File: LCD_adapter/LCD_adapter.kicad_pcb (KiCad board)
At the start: 2 copper layers, 24.8 x 52.1 mm, 3 parts, among them U1 RC1602A

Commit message: version 1 complete
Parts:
- added J1: Conn_01x15_Male, Connector_PinHeader_2.54mm:PinHeader_1x15_P2.54mm_Vertical, F.Cu at (153.7, 64.8)
- added J2: Conn_01x15_Male, Connector_PinHeader_2.54mm:PinHeader_1x15_P2.54mm_Vertical, F.Cu at (163.8, 64.8)
- added REF**: MountingHole_3mm, MountingHole:MountingHole_3mm, F.Cu at (172.0, 61.9)
- added REF**: MountingHole_3mm, MountingHole:MountingHole_3mm, F.Cu at (172.0, 113.7)
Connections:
- A1 pad 1: Net-(A1-Pad1) -> /D1
- A1 pad 10: Net-(A1-Pad10) -> /D7
- A1 pad 11: Net-(A1-Pad11) -> /D8
- A1 pad 12: Net-(A1-Pad12) -> /D9
- A1 pad 13: Net-(A1-Pad13) -> /D10
- A1 pad 16: Net-(A1-Pad16) -> /D13
- A1 pad 17: Net-(A1-Pad17) -> /3V3
- A1 pad 18: Net-(A1-Pad18) -> /AREF
- A1 pad 19: Net-(A1-Pad19) -> /A0
- A1 pad 2: Net-(A1-Pad2) -> /D0
- A1 pad 20: Net-(A1-Pad20) -> /A1
- A1 pad 21: Net-(A1-Pad21) -> /A2
- A1 pad 22: Net-(A1-Pad22) -> /A3
- A1 pad 23: Net-(A1-Pad23) -> /A4
- A1 pad 24: Net-(A1-Pad24) -> /A5
- A1 pad 25: Net-(A1-Pad25) -> /A6
- A1 pad 26: Net-(A1-Pad26) -> /A7
- A1 pad 28: Net-(A1-Pad28) -> /nRST
- A1 pad 3: Net-(A1-Pad3) -> /nRST
- A1 pad 30: Net-(A1-Pad30) -> /Vin
- A1 pad 9: Net-(A1-Pad9) -> /D6
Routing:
- net /nRST: track 0.00 -> 5.08 mm
- net VDD: track 68.1 -> 70.7 mm
- net /D3: track 15.0 -> 17.6 mm
- net /D2: track 15.0 -> 17.6 mm
- net /D12: track 15.0 -> 17.6 mm
- net /Vin: track 0.00 -> 2.54 mm
- net /D9: track 0.00 -> 2.54 mm
- net /D8: track 0.00 -> 2.54 mm, vias 0 -> 1
- net /D7: track 0.00 -> 2.54 mm
- net /D6: track 0.00 -> 2.54 mm
- net /D4: track 15.0 -> 17.6 mm
- net /D13: track 0.00 -> 2.54 mm
- net /D11: track 17.6 -> 20.1 mm
- net /D10: track 0.00 -> 2.54 mm
- net /D1: track 0.00 -> 2.54 mm
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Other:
- board size 24.8 x 52.1 mm -> 26 x 59.1 mm
- board text added: "3V3"
- board text added: "5V"
- board text added: "A0"
- board text added: "A1"
- board text added: "A2"
- board text added: "A3"
- board text added: "A4"
- board text added: "A5"
- board text added: "A6"
- board text added: "A7"
- board text added: "BJI inc. - nano2LCD adapter"
- board text added: "D10"
- board text added: "D11"
- board text added: "D12"
- board text added: "D13"
- board text added: "D2"
- board text added: "D3"
- board text added: "D4"
- board text added: "D5"
- board text added: "D6"
- board text added: "D7"
- board text added: "D8"
- board text added: "D9"
- board text added: "GND"
- board text added: "REF"
- board text added: "RST"
- board text added: "RXD"
- board text added: "TXD"
- board text added: "VIN"

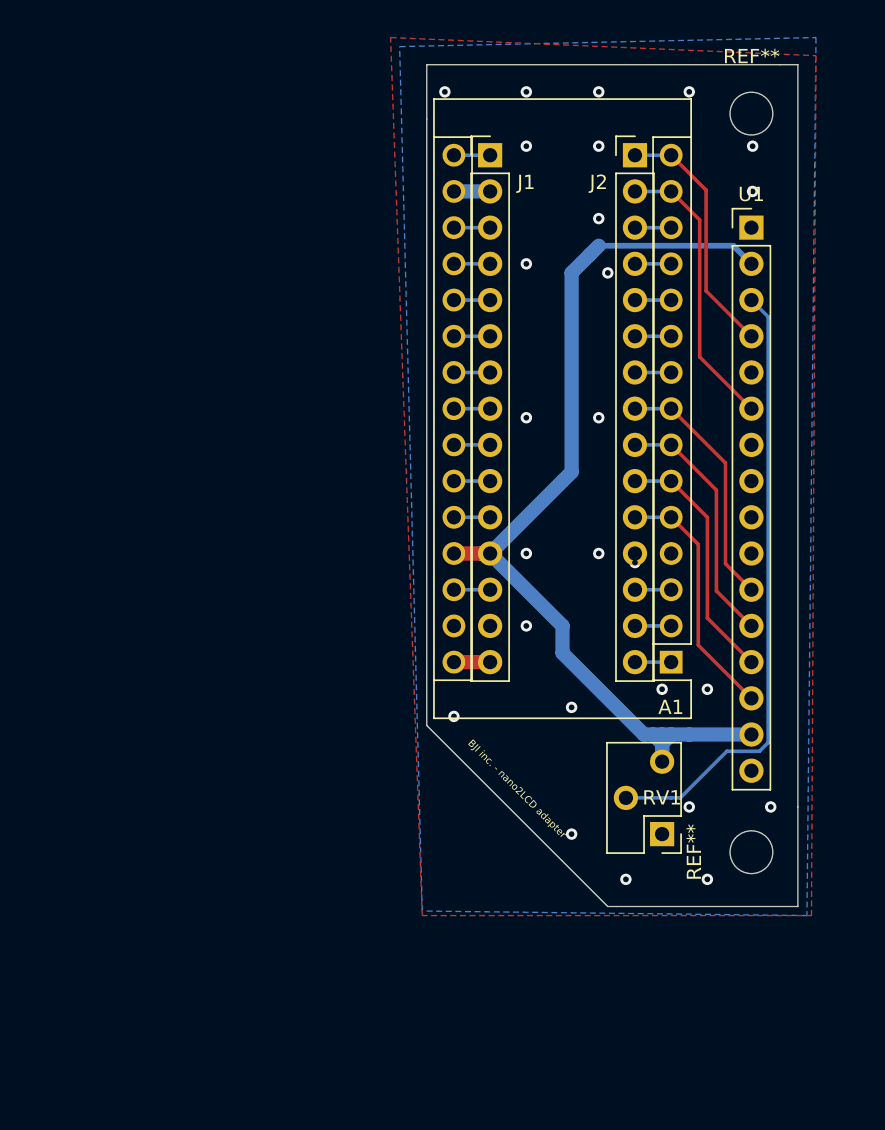
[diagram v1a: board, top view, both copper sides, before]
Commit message: bluetooth module v0 - updated to include the bluetooth module and buttons for control
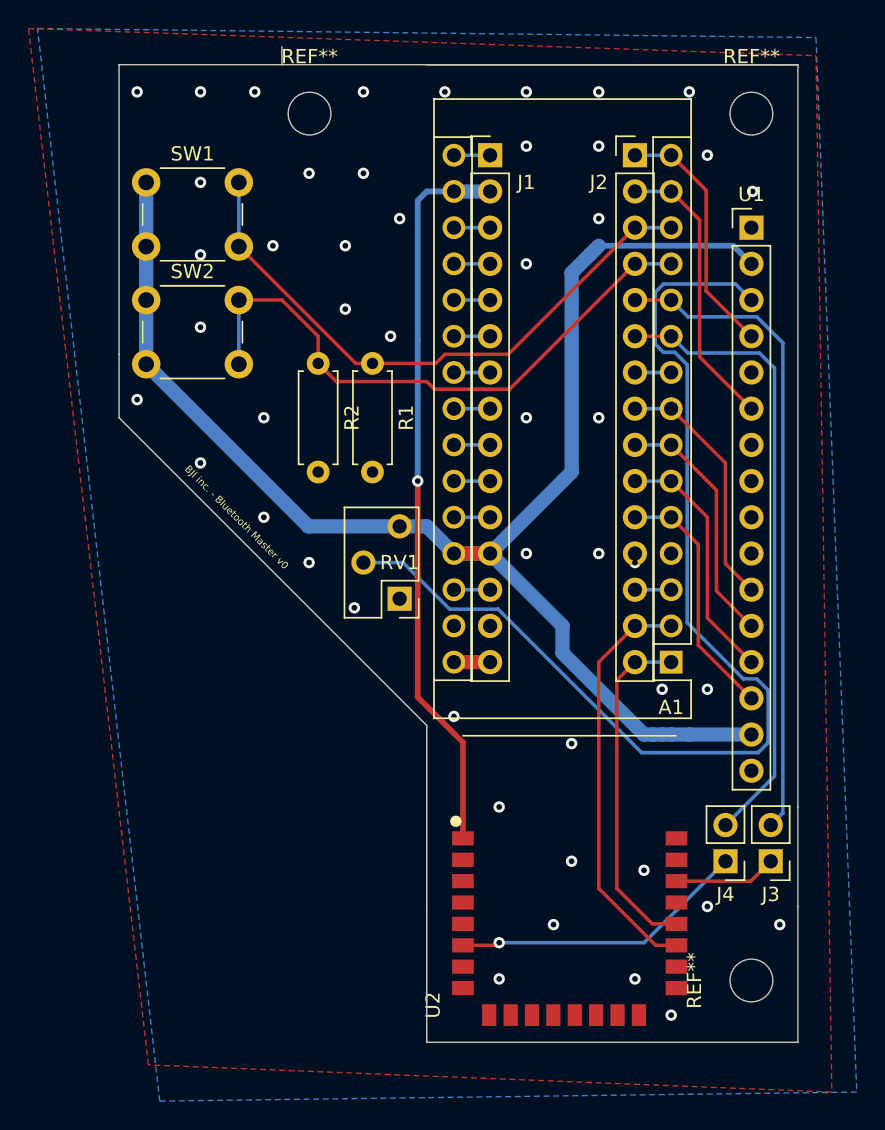
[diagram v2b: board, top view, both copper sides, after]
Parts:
- added J3: Conn_01x02_Male, Connector_PinHeader_2.54mm:PinHeader_1x02_P2.54mm_Vertical, F.Cu at (173.4, 114.3)
- added J4: Conn_01x02_Male, Connector_PinHeader_2.54mm:PinHeader_1x02_P2.54mm_Vertical, F.Cu at (170.2, 114.3)
- added R1: R100k, Resistor_THT:R_Axial_DIN0207_L6.3mm_D2.5mm_P7.62mm_Horizontal, F.Cu at (145.4, 79.4)
- added R2: R100k, Resistor_THT:R_Axial_DIN0207_L6.3mm_D2.5mm_P7.62mm_Horizontal, F.Cu at (141.6, 79.4)
- added REF**: MountingHole_3mm, MountingHole:MountingHole_3mm, F.Cu at (141.0, 61.9)
- added SW1: SW_DIP_x02, brad_footprints:SW_PUSH_6mm_H9.5mm, F.Cu at (129.5, 66.7)
- added SW2: SW_DIP_x02, brad_footprints:SW_PUSH_6mm_H9.5mm, F.Cu at (129.5, 74.9)
- added U2: JDY-16, brad_footprints:JDY-16, F.Cu at (151.8, 125.1)
- moved RV1 24.7 mm to (147.3, 95.9)
- moved REF** 9.00 mm to (172.0, 122.7)
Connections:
- net /3V3 renamed +3V3
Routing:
- net +3V3: track 2.54 -> 51.4 mm, vias 0 -> 1
- net /D8: track 2.54 -> 45.8 mm
- net /D7: track 2.54 -> 44.2 mm
- net /D9: track 2.54 -> 42.3 mm
- net /D10: track 2.54 -> 42.2 mm
- net VDD: track 70.7 -> 105.6 mm
- net Net-(RV1-Pad2): track 43.2 -> 77.6 mm
- net /D0: track 2.54 -> 29.1 mm
- net /D1: track 2.54 -> 24.2 mm
- net /STAT: track 0.00 -> 20.9 mm, vias 0 -> 1
- net /PWRC: track 0.00 -> 7.19 mm
- net GND: vias 27 -> 49
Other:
- board size 26 x 59.1 mm -> 47.6 x 69.8 mm
- board text added: "BJI inc. - Bluetooth Master v0"
- board text removed: "BJI inc. - nano2LCD adapter"

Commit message: fixed for DRC errors
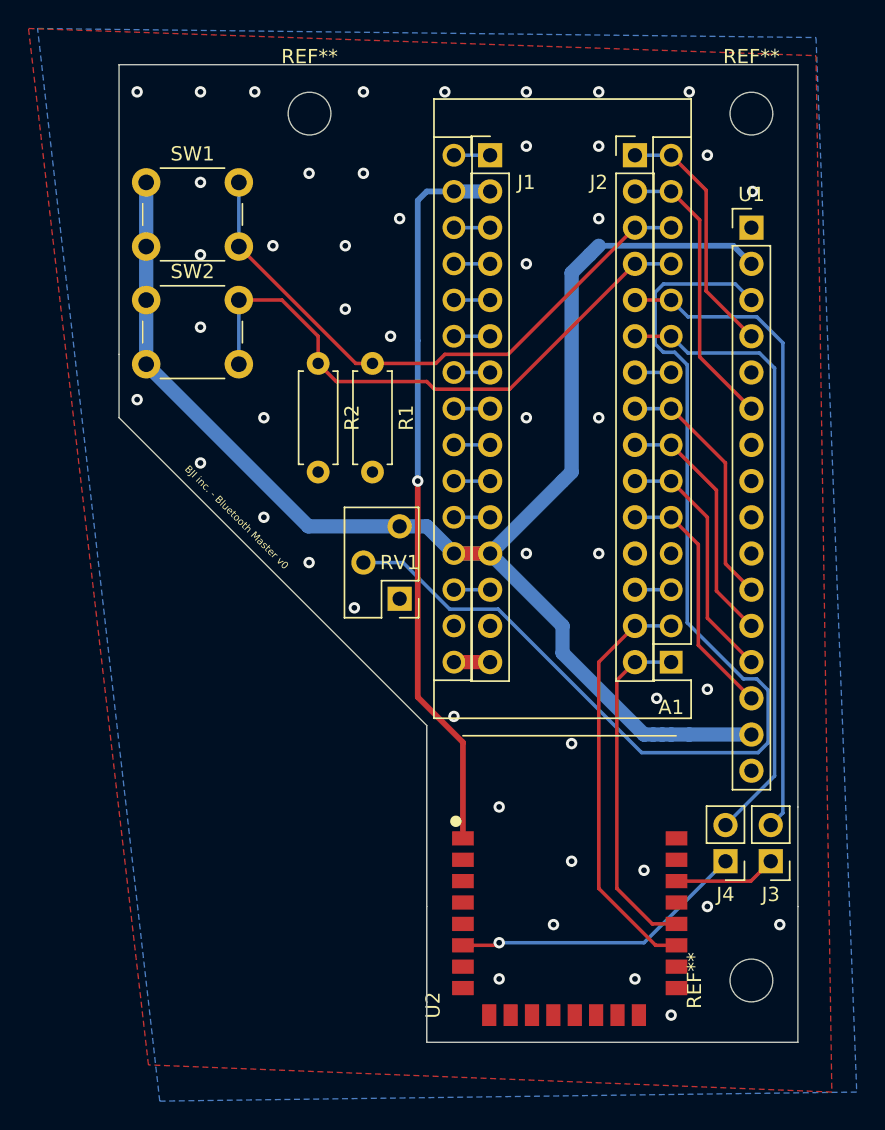
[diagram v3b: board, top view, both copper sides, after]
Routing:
- net GND: vias 49 -> 48
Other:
- board size 47.6 x 69.8 mm -> 47.6 x 68.6 mm
